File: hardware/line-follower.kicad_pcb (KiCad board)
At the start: 2 copper layers, 40 parts, among them U1 QRE1113GR, U10 QRE1113GR, U2 QRE1113GR, U3 QRE1113GR, U4 QRE1113GR, U5 QRE1113GR, U6 QRE1113GR, U7 QRE1113GR, U8 QRE1113GR, U9 QRE1113GR

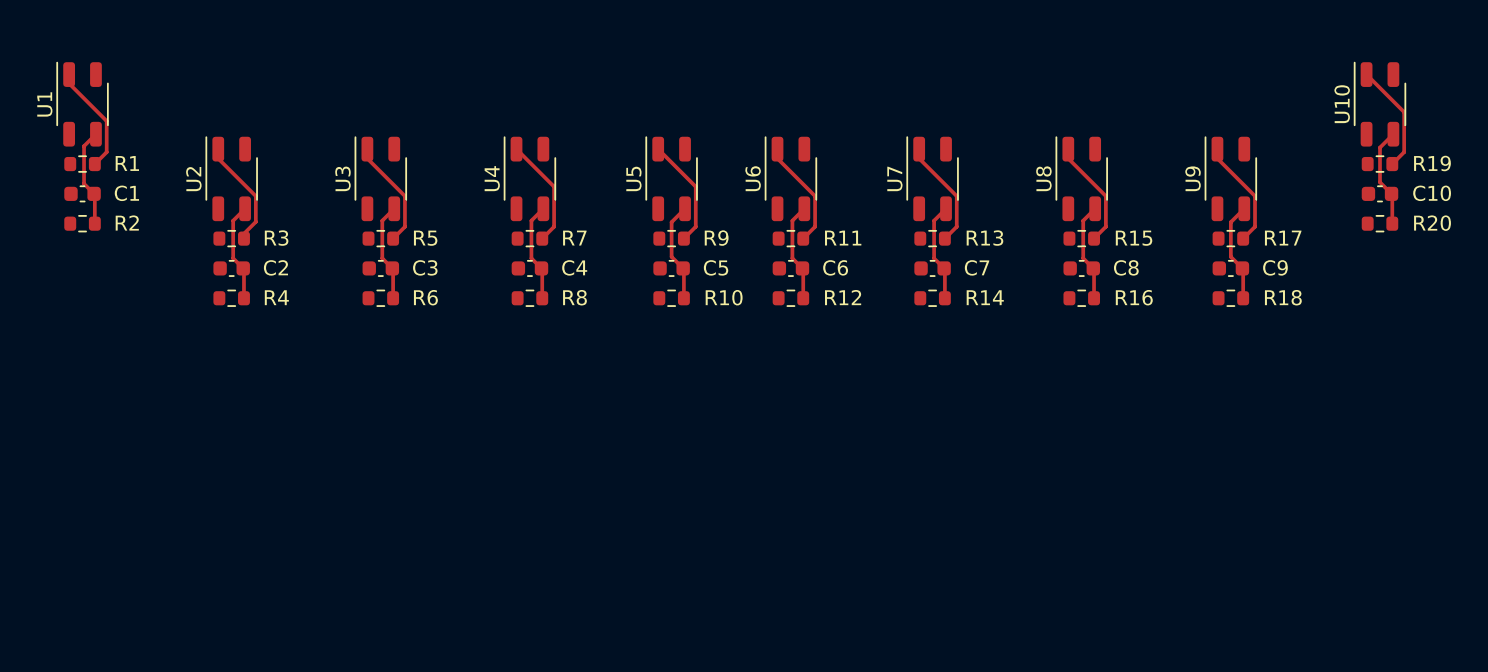
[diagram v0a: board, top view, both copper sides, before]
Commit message: array wiring
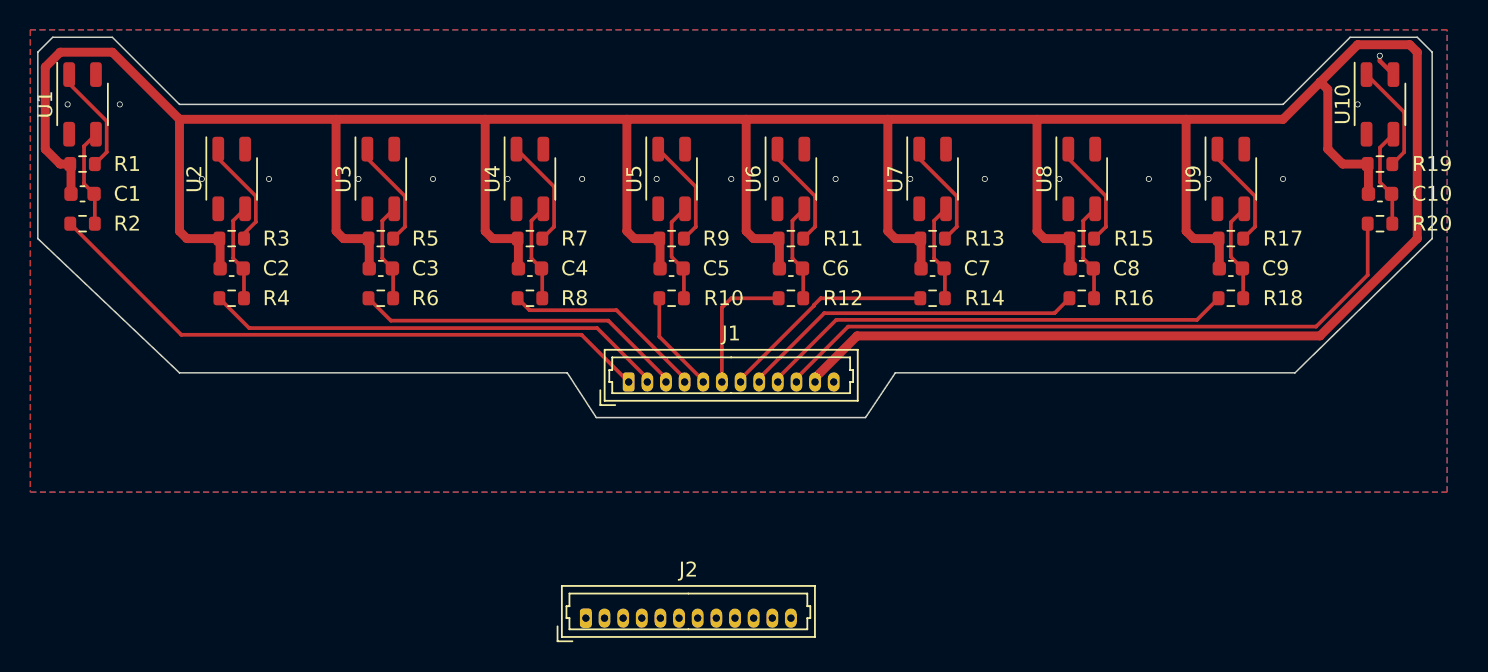
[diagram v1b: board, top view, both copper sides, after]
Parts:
- added J1: Conn_01x12, Connector_Molex:Molex_PicoBlade_53047-1210_1x12_P1.25mm_Vertical, F.Cu at (93.1, 73.6)
- added J2: Conn_01x12, Connector_Molex:Molex_PicoBlade_53047-1210_1x12_P1.25mm_Vertical, F.Cu at (90.2, 89.5)
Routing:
- net +5V: track 0.00 -> 268.7 mm
- net OUT10: track 0.00 -> 44.9 mm
- net OUT1: track 0.00 -> 41.8 mm
- net OUT9: track 0.00 -> 32.0 mm
- net OUT2: track 0.00 -> 31.2 mm
- net OUT8: track 0.00 -> 23.3 mm
- net OUT3: track 0.00 -> 22.4 mm
- net OUT7: track 0.00 -> 14.5 mm
- net OUT4: track 0.00 -> 13.7 mm
- net OUT6: track 0.00 -> 9.05 mm
- net OUT5: track 0.00 -> 6.94 mm
- net GND: track 0.00 -> 1.64 mm, vias 0 -> 20
- added copper zone on B.Cu, net GND
- added copper zone on F.Cu, net GND
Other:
- board outline added: 93.5 x 25.5 mm

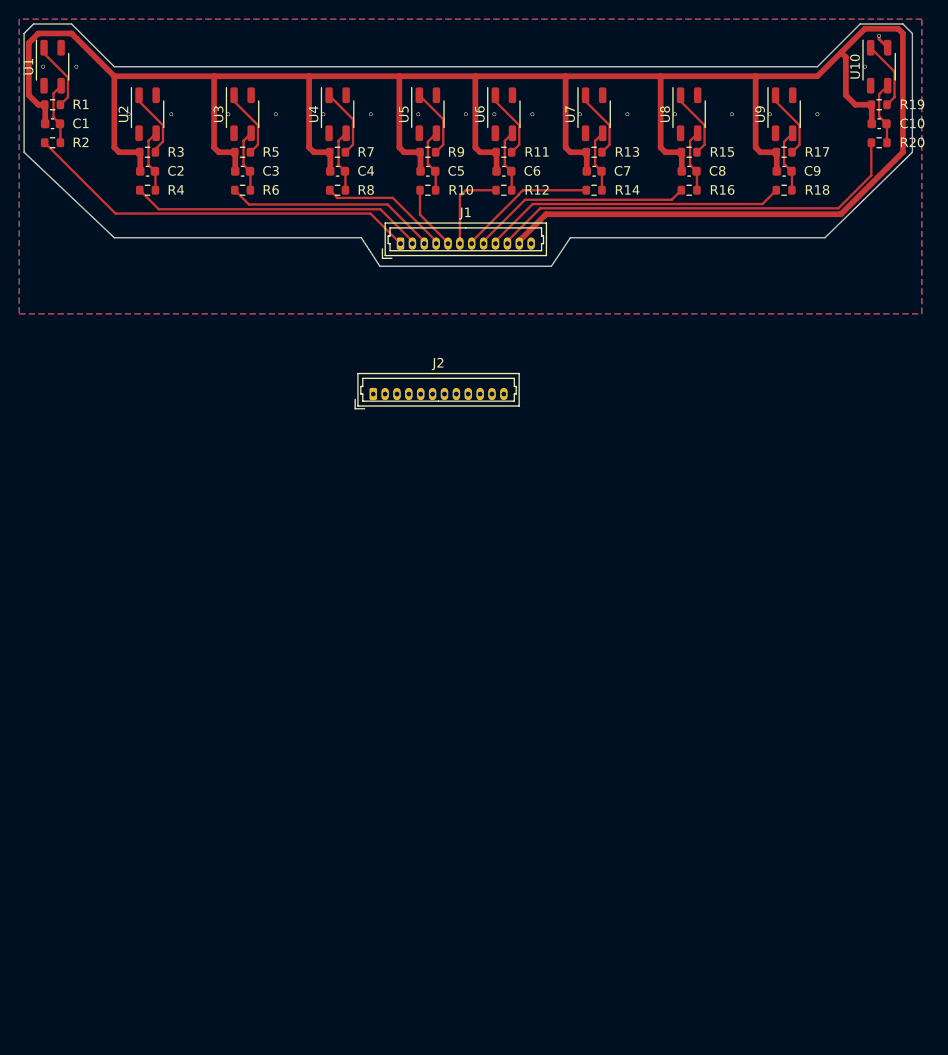
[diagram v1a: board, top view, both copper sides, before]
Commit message: add hole for fan
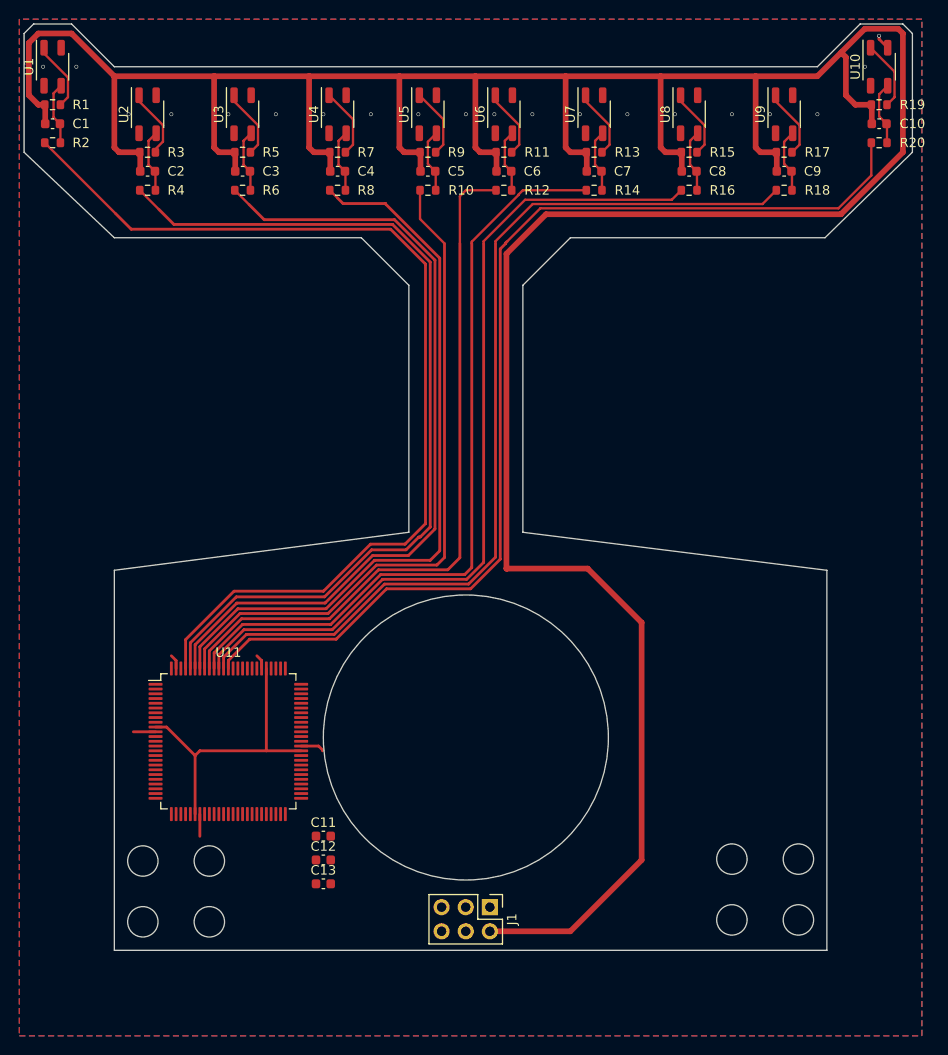
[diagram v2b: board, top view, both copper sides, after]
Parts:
- removed J2: Conn_01x12, Connector_Molex:Molex_PicoBlade_53047-1210_1x12_P1.25mm_Vertical
- added C11: 10nF, Capacitor_SMD:C_0603_1608Metric, F.Cu at (85.0, 136.0)
- added C12: 10nF, Capacitor_SMD:C_0603_1608Metric, F.Cu at (85.0, 138.5)
- added C13: 10nF, Capacitor_SMD:C_0603_1608Metric, F.Cu at (85.0, 141.0)
- added U11: ATmega2560-16A, Package_QFP:TQFP-100_14x14mm_P0.5mm, F.Cu at (75.0, 126.0)
- J1: value Conn_01x12 -> AVR-ISP-6; footprint Connector_Molex:Molex_PicoBlade_53047-1210_1x12_P1.25mm_Vertical -> Connector_PinHeader_2.54mm:PinHeader_2x03_P2.54mm_Vertical
- moved J1 70.5 mm to (102.5, 143.5), turned to -90 degrees
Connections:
- J1 pad 1: OUT1 -> MISO
- J1 pad 2: OUT2 -> +5V
- J1 pad 3: OUT3 -> SCK
- J1 pad 4: OUT4 -> MOSI
- J1 pad 5: OUT5 -> RESET
- J1 pad 6: OUT6 -> GND
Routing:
- net +5V: track 268.7 -> 364.2 mm
- net OUT10: track 44.9 -> 112.3 mm
- net OUT9: track 32.0 -> 99.2 mm
- net OUT8: track 23.3 -> 90.2 mm
- net OUT7: track 14.5 -> 81.1 mm
- net OUT6: track 9.05 -> 74.4 mm
- net OUT1: track 41.8 -> 106.0 mm
- net OUT5: track 6.94 -> 71.1 mm
- net OUT2: track 31.2 -> 94.6 mm
- net OUT4: track 13.7 -> 77.1 mm
- net OUT3: track 22.4 -> 85.2 mm
- net Net-(C11-Pad2): track 0.00 -> 31.6 mm
- net GND: track 1.64 -> 11.9 mm
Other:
- board size 93.5 x 25.5 mm -> 93.5 x 97.5 mm

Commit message: add regulator
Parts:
- added C14: C_Polarized_Small, Capacitor_SMD:CP_Elec_6.3x4.9, F.Cu at (123.0, 114.0)
- added C15: C_Polarized_Small, Capacitor_SMD:CP_Elec_6.3x4.9, F.Cu at (132.0, 114.0)
- added C16: 20p, Capacitor_SMD:C_0603_1608Metric, F.Cu at (84.7, 141.2)
- added C17: 20p, Capacitor_SMD:C_0603_1608Metric, F.Cu at (81.1, 141.2)
- added C18: 10nF, Capacitor_SMD:C_0603_1608Metric, F.Cu at (123.2, 93.0)
- added C19: 10nF, Capacitor_SMD:C_0603_1608Metric, F.Cu at (123.2, 95.5)
- added C20: 10nF, Capacitor_SMD:C_0603_1608Metric, F.Cu at (123.2, 98.0)
- added C21: C_Polarized_Small, Capacitor_SMD:CP_Elec_6.3x4.9, F.Cu at (135.4, 100.8)
- added D1: 1N5819, Diode_THT:D_DO-41_SOD81_P10.16mm_Horizontal, F.Cu at (119.5, 131.1)
- added J2: Conn_01x02, Connector_PinSocket_2.54mm:PinSocket_1x02_P2.54mm_Vertical, F.Cu at (132.0, 131.0)
- added J3: Conn_01x02, Connector_PinSocket_2.54mm:PinSocket_1x02_P2.54mm_Vertical, F.Cu at (125.5, 131.0)
- added J4: Conn_01x02, Connector_PinHeader_2.54mm:PinHeader_1x02_P2.54mm_Vertical, F.Cu at (119.0, 137.0)
- added Q1: Si2319CDS, Package_TO_SOT_SMD:SOT-23, F.Cu at (123.4, 138.2)
- added R21: 1M, Resistor_SMD:R_0603_1608Metric, F.Cu at (73.2, 135.7)
- added R22: R_Small, Resistor_SMD:R_0603_1608Metric, F.Cu at (123.6, 142.4)
- added R23: R_Small, Resistor_SMD:R_0603_1608Metric, F.Cu at (123.6, 140.8)
- added U12: MX1508, Package_SO:SOIC-16W_5.3x10.2mm_P1.27mm, F.Cu at (127.0, 124.0)
- added U13: LM317_SOT-223, Package_TO_SOT_SMD:SOT-223-3_TabPin2, F.Cu at (117.0, 144.2)
- added Y1: Crystal, Crystal:Crystal_SMD_HC49-SD, F.Cu at (81.5, 137.5)
- U1, U10, U2, U3, U4, U5, U6, U7, U8, U9: moved to B.Cu
- moved C12 28.0 mm to (68.4, 116.0), turned to 180 degrees
- moved C11 22.8 mm to (65.0, 125.1), turned to 90 degrees
- moved C13 9.31 mm to (84.5, 131.7), turned to 90 degrees
- turned U1 to 180 degrees
- turned U10 to 180 degrees
- turned U2 to 180 degrees
- turned U3 to 180 degrees
- turned U4 to 180 degrees
- turned U5 to 180 degrees
- turned U6 to 180 degrees
- turned U7 to 180 degrees
- turned U8 to 180 degrees
- turned U9 to 180 degrees
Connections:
- C11 pad 1: unconnected-(C11-Pad1) -> GND
- C11 pad 2: Net-(C11-Pad2) -> +5V
- C12 pad 1: unconnected-(C12-Pad1) -> GND
- C12 pad 2: Net-(C11-Pad2) -> +5V
- C13 pad 1: unconnected-(C13-Pad1) -> GND
- C13 pad 2: Net-(C11-Pad2) -> +5V
- U11 pad 10: Net-(C11-Pad2) -> +5V
- U11 pad 100: unconnected-(U11-AVCC-Pad100) -> +5V
- U11 pad 15: unconnected-(U11-PH3-Pad15) -> MOTOR_L_A
- U11 pad 16: unconnected-(U11-PH4-Pad16) -> MOTOR_L_B
- U11 pad 17: unconnected-(U11-PH5-Pad17) -> MOTOR_R_A
- U11 pad 18: unconnected-(U11-PH6-Pad18) -> MOTOR_R_B
- U11 pad 20: unconnected-(U11-PB1-Pad20) -> SCK
- U11 pad 21: unconnected-(U11-PB2-Pad21) -> MOSI
- U11 pad 22: unconnected-(U11-PB3-Pad22) -> MISO
- U11 pad 23: unconnected-(U11-PB4-Pad23) -> MOTOR_1
- U11 pad 30: unconnected-(U11-~{RESET}-Pad30) -> RESET
- U11 pad 31: Net-(C11-Pad2) -> +5V
- U11 pad 33: unconnected-(U11-XTAL2-Pad33) -> OSOUT
- U11 pad 34: unconnected-(U11-XTAL1-Pad34) -> OSIN
- U11 pad 61: Net-(C11-Pad2) -> +5V
- U11 pad 80: Net-(C11-Pad2) -> +5V
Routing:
- net +5V: track 364.2 -> 497.0 mm
- net MOTOR_L_A: track 0.00 -> 79.0 mm, vias 0 -> 2
- net MOTOR_L_B: track 0.00 -> 77.9 mm, vias 0 -> 2
- net MOTOR_R_B: track 0.00 -> 75.1 mm, vias 0 -> 2
- net MOTOR_R_A: track 0.00 -> 74.0 mm, vias 0 -> 2
- net MOTOR_1: track 0.00 -> 61.6 mm, vias 0 -> 2
- net SCK: track 0.00 -> 54.5 mm
- net MISO: track 0.00 -> 49.7 mm
- net MOSI: track 0.00 -> 48.1 mm
- net RESET: track 0.00 -> 34.4 mm
- net Net-(C11-Pad2): track 31.6 -> 0.00 mm
- net Net-(D1-A): track 0.00 -> 20.5 mm
- net OSOUT: track 0.00 -> 20.1 mm
- net OSIN: track 0.00 -> 19.5 mm
- net +BATT: track 0.00 -> 8.18 mm
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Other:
- outline, holes or cut-outs redrawn

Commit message: add battery connector
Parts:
- added D2: LED, LED_SMD:LED_0603_1608Metric, B.Cu at (71.5, 58.6)
- added D3: LED, LED_SMD:LED_0603_1608Metric, B.Cu at (81.5, 58.5)
- added D4: LED, LED_SMD:LED_0603_1608Metric, B.Cu at (91.0, 58.5)
- added D5: LED, LED_SMD:LED_0603_1608Metric, B.Cu at (109.0, 58.5)
- added D6: LED, LED_SMD:LED_0603_1608Metric, B.Cu at (118.5, 58.5)
- added D7: LED, LED_SMD:LED_0603_1608Metric, B.Cu at (128.5, 58.5)
- added J5: Conn_01x02, Connector_TE-Connectivity:TE_826576-2_1x02_P3.96mm_Vertical, F.Cu at (129.5, 134.5)
- added Q2: 2N7002, Package_TO_SOT_SMD:SOT-23, F.Cu at (137.5, 58.8)
- added R24: 2K, Resistor_SMD:R_0603_1608Metric, F.Cu at (71.5, 62.5)
- added R25: 2K, Resistor_SMD:R_0603_1608Metric, F.Cu at (81.5, 62.5)
- added R26: 2K, Resistor_SMD:R_0603_1608Metric, F.Cu at (91.0, 62.5)
- added R27: 2K, Resistor_SMD:R_0603_1608Metric, F.Cu at (109.0, 62.5)
- added R28: 2K, Resistor_SMD:R_0603_1608Metric, F.Cu at (118.5, 62.5)
- added R29: 2K, Resistor_SMD:R_0603_1608Metric, F.Cu at (128.5, 62.5)
- added R30: 10K, Resistor_SMD:R_0603_1608Metric, F.Cu at (136.5, 62.2)
- added R31: 2K, Resistor_SMD:R_0603_1608Metric, F.Cu at (140.0, 61.5)
- moved C18 52.0 mm to (122.6, 145.0), turned to 90 degrees
- moved C20 50.6 mm to (110.6, 147.0)
- moved C19 49.5 mm to (124.4, 145.0), turned to 90 degrees
- moved C21 20.6 mm to (119.6, 114.0), turned to 90 degrees
- moved C14 3.80 mm to (126.8, 114.0), turned to 90 degrees
- moved C15 2.20 mm to (134.2, 114.0), turned to 90 degrees
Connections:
- U11 pad 87: unconnected-(U11-PK2-Pad87) -> F_LED
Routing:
- net F_LED: track 0.00 -> 112.6 mm
- net Net-(D2-A): track 0.00 -> 81.3 mm, vias 0 -> 1
- net +BATT: track 8.18 -> 47.9 mm, vias 0 -> 1
- net +5V: track 497.0 -> 504.7 mm
- net Net-(Q2-G): track 0.00 -> 4.46 mm
- net MOTOR_R_B: track 75.1 -> 72.7 mm
- net Net-(D6-K): track 0.00 -> 2.39 mm, vias 0 -> 1
- net Net-(D5-K): track 0.00 -> 2.39 mm, vias 0 -> 1
- net Net-(D4-K): track 0.00 -> 2.39 mm, vias 0 -> 1
- net Net-(D3-K): track 0.00 -> 2.39 mm, vias 0 -> 1
- net Net-(D7-K): track 0.00 -> 2.35 mm, vias 0 -> 1
- net Net-(D2-K): track 0.00 -> 2.29 mm, vias 0 -> 1
- net MOTOR_L_B: track 77.9 -> 76.5 mm
- net MOTOR_L_A: track 79.0 -> 77.9 mm
- net OUT9: track 96.1 -> 96.9 mm
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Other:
- outline, holes or cut-outs redrawn

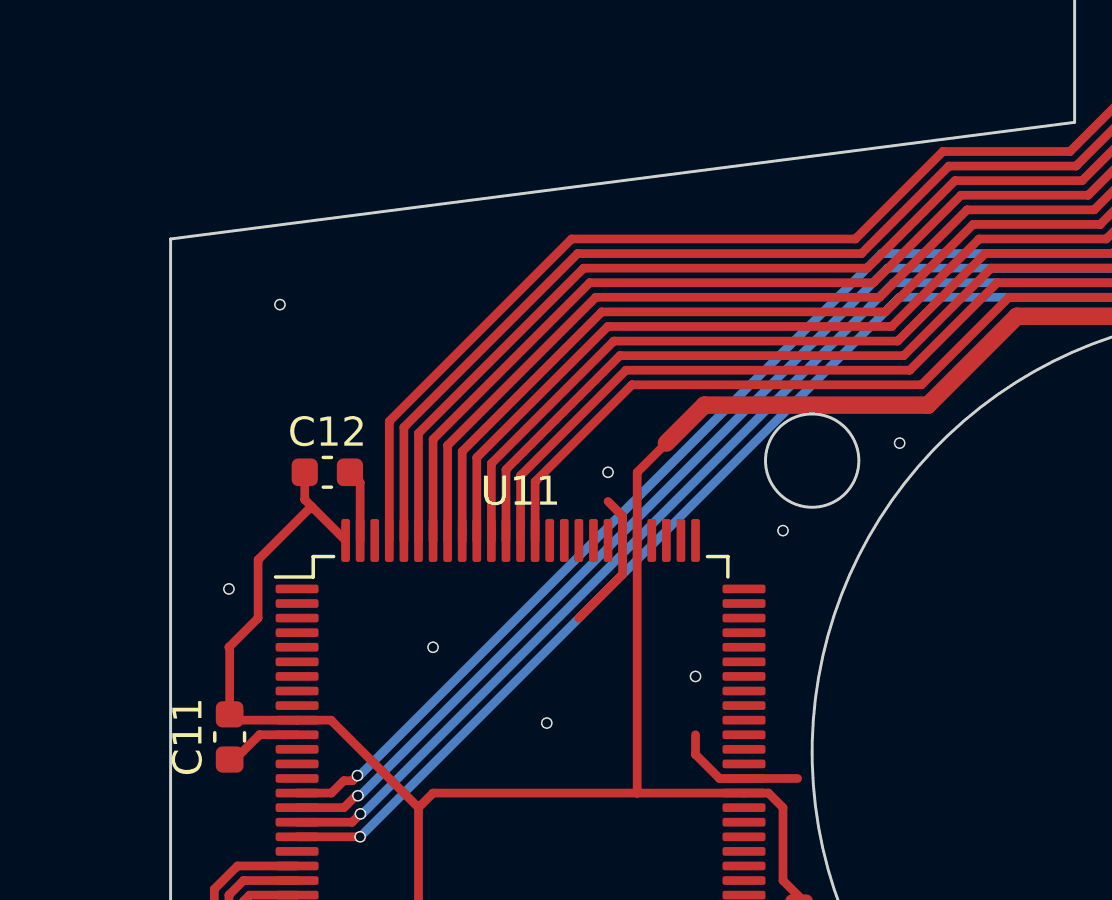
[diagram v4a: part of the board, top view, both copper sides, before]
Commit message: add led + switch
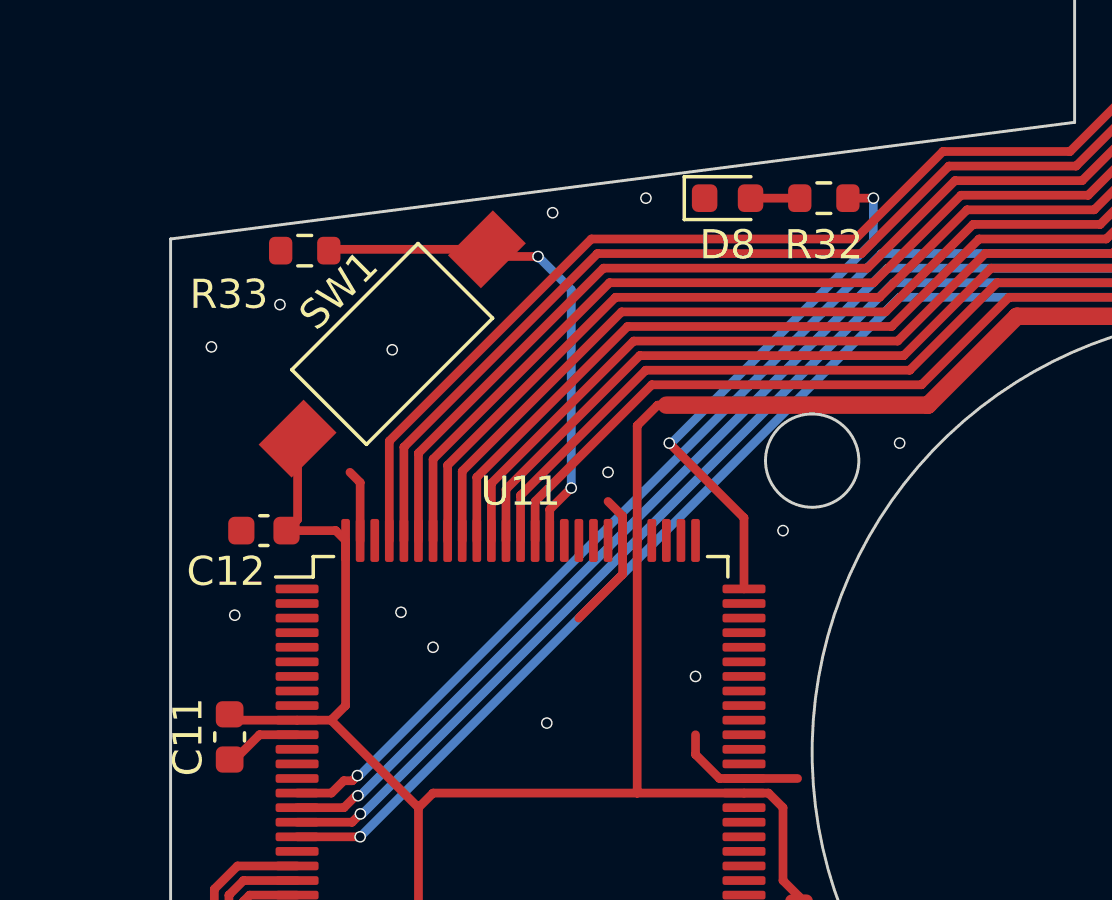
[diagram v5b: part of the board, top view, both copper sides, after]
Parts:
- added D8: LED, LED_SMD:LED_0603_1608Metric, F.Cu at (82.1, 106.6)
- added R32: 1K1, Resistor_SMD:R_0603_1608Metric, F.Cu at (85.4, 106.6)
- added R33: 10K, Resistor_SMD:R_0603_1608Metric, F.Cu at (67.6, 108.4)
- added SW1: SW_SPST, Button_Switch_SMD:SW_SPST_FSMSM, F.Cu at (70.6, 111.6)
- moved C12 2.95 mm to (66.2, 118.0), turned to 0 degrees
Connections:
- U11 pad 43: unconnected-(U11-PD0-Pad43) -> SCL
- U11 pad 44: unconnected-(U11-PD1-Pad44) -> SDA
- U11 pad 75: unconnected-(U11-PA3-Pad75) -> LED1
- U11 pad 85: unconnected-(U11-PK4-Pad85) -> BTN2
- U11 pad 86: unconnected-(U11-PK3-Pad86) -> BTN1
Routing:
- net LED1: track 0.00 -> 18.3 mm, vias 0 -> 2
- net BTN1: track 0.00 -> 17.8 mm, vias 0 -> 2
- net Net-(D8-A): track 0.00 -> 1.69 mm
- net +5V: track 504.7 -> 506.3 mm
- net GND: vias 66 -> 71
